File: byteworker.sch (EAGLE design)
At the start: 48 parts, among them IC1 MCP1703, IC2 TJA1043, J1 AVRSPI-62.56-H, Q1 BSS138, Q2 BSS138, Q5 BSS138, Q6 FDN5618P, X1 16 MHz, X2 bus connector

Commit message: unknown changes on IC2
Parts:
- removed C8: 100n, bytewerk-passive:C0603
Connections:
- net +5V: no longer C8.1
- net GND: no longer C8.2
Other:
- moved on the sheet: C7, IC2PWR
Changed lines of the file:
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@@
 <part name="GND10" library="supply1" deviceset="GND" device=""/>
 <part name="C7" library="bytewerk-passive" deviceset="C" device="0603" value="100n"/>
-<part name="C8" library="bytewerk-passive" deviceset="C" device="0603" value="100n"/>
 <part name="GND11" library="supply1" deviceset="GND" device=""/>
-<part name="GND12" library="supply1" deviceset="GND" device=""/>
 <part name="TP1" library="testpad" deviceset="PTR1" device="TP10SQ"/>
 <part name="C3" library="bytewerk-rcl" deviceset="C" device="1206" value="1u/10v"/>
@@
 <instance part="GND15" gate="1" x="106.68" y="50.8"/>
 <instance part="R20" gate="G$1" x="165.1" y="53.34"/>
-<instance part="IC2" gate="PWR" x="10.16" y="71.12" rot="MR0"/>
-<instance part="GND10" gate="1" x="22.86" y="58.42" rot="MR0"/>
-<instance part="C7" gate="G$1" x="27.94" y="66.04" rot="MR270"/>
-<instance part="C8" gate="G$1" x="33.02" y="66.04" rot="MR270"/>
-<instance part="GND11" gate="1" x="27.94" y="58.42" rot="MR0"/>
-<instance part="GND12" gate="1" x="33.02" y="58.42" rot="MR0"/>
+<instance part="IC2" gate="PWR" x="35.56" y="73.66" rot="MR0"/>
+<instance part="GND10" gate="1" x="48.26" y="60.96" rot="MR0"/>
+<instance part="C7" gate="G$1" x="53.34" y="68.58" rot="MR270"/>
+<instance part="GND11" gate="1" x="53.34" y="60.96" rot="MR0"/>
 <instance part="JUMPER1" gate="G$1" x="175.26" y="91.44" rot="R270"/>
 <instance part="D4" gate="G$1" x="218.44" y="81.28" rot="R180"/>
@@
 <segment>
 <pinref part="IC2" gate="PWR" pin="GND"/>
-<wire x1="20.32" y1="68.58" x2="22.86" y2="68.58" width="0.1524" layer="91"/>
-<wire x1="22.86" y1="68.58" x2="22.86" y2="60.96" width="0.1524" layer="91"/>
+<wire x1="45.72" y1="71.12" x2="48.26" y2="71.12" width="0.1524" layer="91"/>
+<wire x1="48.26" y1="71.12" x2="48.26" y2="63.5" width="0.1524" layer="91"/>
 <pinref part="GND10" gate="1" pin="GND"/>
 </segment>
@@
 <pinref part="C7" gate="G$1" pin="2"/>
 <pinref part="GND11" gate="1" pin="GND"/>
-<wire x1="27.94" y1="60.96" x2="27.94" y2="63.5" width="0.1524" layer="91"/>
-</segment>
-<segment>
-<pinref part="C8" gate="G$1" pin="2"/>
-<pinref part="GND12" gate="1" pin="GND"/>
-<wire x1="33.02" y1="60.96" x2="33.02" y2="63.5" width="0.1524" layer="91"/>
+<wire x1="53.34" y1="63.5" x2="53.34" y2="66.04" width="0.1524" layer="91"/>
 </segment>
 <segment>
@@
 </segment>
 <segment>
+<pinref part="IC2" gate="PWR" pin="VIO"/>
+<wire x1="45.72" y1="76.2" x2="53.34" y2="76.2" width="0.1524" layer="91"/>
+<pinref part="C7" gate="G$1" pin="1"/>
+<wire x1="53.34" y1="73.66" x2="53.34" y2="76.2" width="0.1524" layer="91"/>
+<junction x="53.34" y="76.2"/>
 <pinref part="IC2" gate="PWR" pin="VCC"/>
-<wire x1="20.32" y1="76.2" x2="33.02" y2="76.2" width="0.1524" layer="91"/>
-<pinref part="C8" gate="G$1" pin="1"/>
-<wire x1="33.02" y1="76.2" x2="50.8" y2="76.2" width="0.1524" layer="91"/>
-<wire x1="33.02" y1="71.12" x2="33.02" y2="76.2" width="0.1524" layer="91"/>
-<junction x="33.02" y="76.2"/>
-<label x="22.86" y="76.2" size="1.778" layer="95"/>
-</segment>
-<segment>
-<pinref part="IC2" gate="PWR" pin="VIO"/>
-<wire x1="20.32" y1="73.66" x2="27.94" y2="73.66" width="0.1524" layer="91"/>
-<pinref part="C7" gate="G$1" pin="1"/>
-<wire x1="27.94" y1="73.66" x2="50.8" y2="73.66" width="0.1524" layer="91"/>
-<wire x1="27.94" y1="71.12" x2="27.94" y2="73.66" width="0.1524" layer="91"/>
-<junction x="27.94" y="73.66"/>
-<label x="22.86" y="73.66" size="1.778" layer="95"/>
+<wire x1="45.72" y1="78.74" x2="53.34" y2="78.74" width="0.1524" layer="91"/>
+<wire x1="53.34" y1="78.74" x2="58.42" y2="78.74" width="0.1524" layer="91"/>
+<wire x1="58.42" y1="78.74" x2="76.2" y2="78.74" width="0.1524" layer="91"/>
+<label x="48.26" y="78.74" size="1.778" layer="95"/>
+<wire x1="53.34" y1="76.2" x2="53.34" y2="78.74" width="0.1524" layer="91"/>
+<junction x="53.34" y="78.74"/>
 </segment>
 </net>
@@
 <segment>
 <pinref part="IC2" gate="PWR" pin="VBAT"/>
-<wire x1="20.32" y1="78.74" x2="50.8" y2="78.74" width="0.1524" layer="91"/>
-<label x="22.86" y="78.74" size="1.778" layer="95"/>
-</segment>
-<segment>
+<wire x1="45.72" y1="81.28" x2="76.2" y2="81.28" width="0.1524" layer="91"/>
+<label x="48.26" y="81.28" size="1.778" layer="95"/>
+</segment>
+<segment>

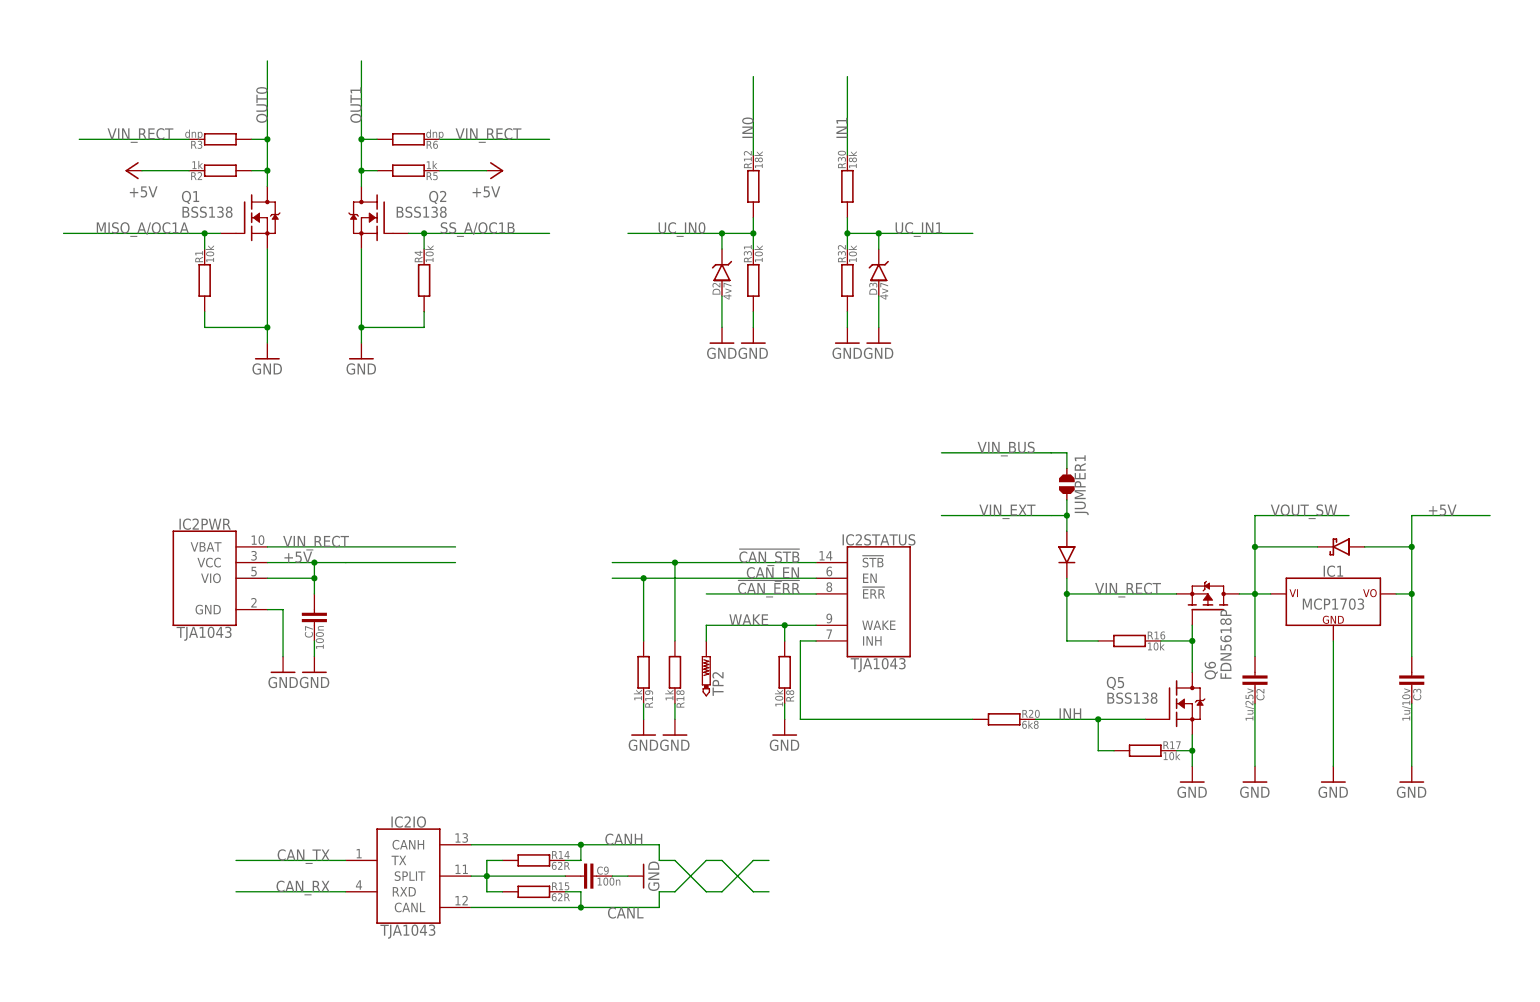
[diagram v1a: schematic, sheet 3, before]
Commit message: - 3rd output fet - moved one ISP pin away from output FET - larger connector with additional ground - larger capacitors - lower part count
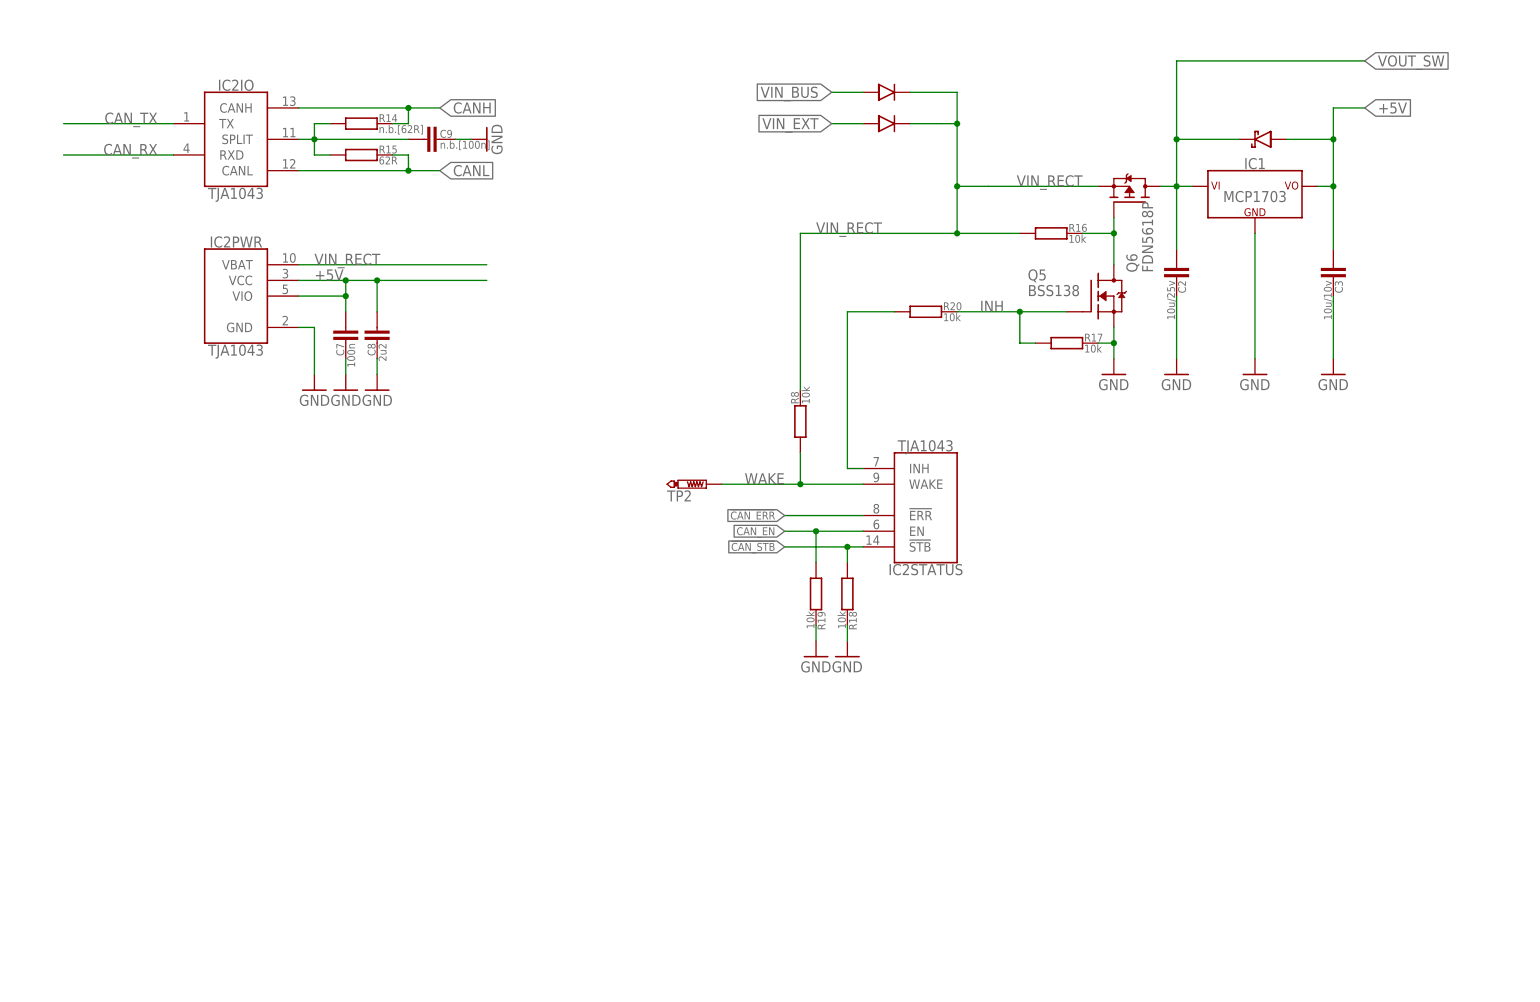
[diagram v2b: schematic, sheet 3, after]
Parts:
- removed JP1: I/O, pinhead:PINHD-2X5/90
- removed JUMPER1: JUMPER-2_10B, bytewerk-jumper:JUMPER-2_10B
- added C8: 2u2, bytewerk-passive:C0805
- added D5: 1N5819HW, bytewerk-passive:1N5819HW
- added JP2: (no value), pinhead:PINHD-2X8/90
- added Q3: BSS138, bytewerk-fet:BSS138
- added R10, R9: 10k, bytewerk-rcl:R0603
- added R11: dnp, bytewerk-rcl:R0603
- added TP3: PTR1TP10SQ, testpad:PTR1TP10SQ
- C2: value 1u/25v -> 10u/25v
- C3: value 1u/10v -> 10u/10v
- C9: value 100n -> n.b.[100n]
- R14: value 62R -> n.b.[62R]
- R18, R19, R2, R5: value 1k -> 10k
- R20: value 6k8 -> 10k
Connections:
- net TXD/MOSI_A/OC0A renamed TXD/MOSI_A/OC0A/SS
- new net N$9: TP3.TP, UC1PORTD.(PSCIN0/CLKO)PD1
- new net OUT2: JP2.9, Q3.D, R10.1, R11.1
- new net PB6: Q1.G, R1.2, UC1PORTB.(ADC7/PSCOUT1B)PB6
- new net PD5/ADC2: JP2.10, UC1PORTD.(ADC2/ACMP2)PD5
- new net PD6/ADC3: JP2.12, UC1PORTD.(ADC3/ACMPN2/INT0)PD6
- new net PD7: Q3.G, R9.2, UC1PORTD.(ACMP0)PD7
- net +5V: now also C8.1, R10.2
- net D2A: now also JP2.14; no longer JP1.10
- net GND: now also C8.2, JP2.16, JP2.2, Q3.S, R9.1; no longer R8.2
- net IN0: now also JP2.4; no longer JP1.6
- net IN1: now also JP2.6; no longer JP1.8
- net MISO_A/OC1A: no longer Q1.G, R1.2
- net OUT0: now also JP2.5; no longer JP1.2
- net OUT1: now also JP2.7; no longer JP1.4
- net PB0/MISO: now also JP2.13; no longer JP1.9
- net PB1/MOSI: now also JP2.15; no longer JP1.7
- net PB7/SCK: now also JP2.11; no longer JP1.5
- net VIN_BUS: now also D5.A; no longer JUMPER1.2
- net VIN_EXT: now also JP2.1; no longer JP1.1, JUMPER1.1
- net VIN_RECT: now also D5.C, R11.2, R8.2
- net VOUT_SW: now also JP2.3; no longer JP1.3
- net WAKE: now also JP2.8
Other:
- note added: "7V to 16V"
- note added: "I/O"
- note added: "MISO/OC1A bereits auf Programmer"
- note removed: "6V to 16V"
- moved on the sheet: C1, C2, C3, C4, C5, C6, C7, C9, IC1, IC2IO, IC2PWR, IC2STATUS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

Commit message: - minor changes to schemanics - placement done(brd)
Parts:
- removed J1: AVRSPI-62.56-H, bytewerk-con:AVRSPI-62.56-H
- removed R7: 1k, bytewerk-passive:R0603
- removed TP1, TP3: PTR1TP10SQ, testpad:PTR1TP10SQ
- added J2: AVRSPI-61.27, bytewerk-con:AVRSPI-61.27
- added JP1, JP3: (no value), pinhead:PINHD-1X10
- added LED2: green, bytewerk-led:LED0603
- added R21, R22: 1k, bytewerk-passive:R0603
- JP2: device pinhead:PINHD-2X8/90 -> pinhead:PINHD-1X8
- X1: device bytewerk-crystal:CRYSTALHC49UP -> bytewerk-crystal:CRYSTAL5X3.2
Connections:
- removed net N$8: LED1.C, R7.1
- removed net N$9: TP3.TP, UC1PORTD.(PSCIN0/CLKO)PD1
- new net N$3: LED2.A, R22.2
- new net PC4: JP3.3, UC1PORTC.(ADC8/AMP1-/ACMPN3)PC4
- new net PD1: JP3.7, UC1PORTD.(PSCIN0/CLKO)PD1
- new net TESTLED1: R21.1, UC1PORTC.(AMP1+/ACMP3/ADC9)PC5
- new net TESTLED2: R22.1, UC1PORTC.(ADC10/ACMP1)PC6
- new net TESTLED3: UC1PORTD.(PSCOUT0A)PD0
- net !RESET!: now also J2.RESET, JP1.10; no longer J1.RESET
- net +5V: now also J2.+5V, JP3.4; no longer J1.+5V
- net AREF: no longer TP1.TP
- net CANH: now also JP3.9
- net CANL: now also JP3.8
- net D2A: now also JP3.6; no longer JP2.14
- net GND: now also J2.GND, JP1.1, JP2.8, LED1.C, LED2.C; no longer J1.GND, JP2.16, JP2.2, R7.2
- net IN0: now also JP2.2; no longer JP2.4
- net IN1: now also JP2.1; no longer JP2.6
- net MISO_A/OC1A: now also J2.MISO, JP1.9; no longer J1.MISO
- net N$7: now also R21.2; no longer UC1PORTD.(PSCOUT0A)PD0
- net OUT0: now also JP2.7; no longer JP2.5
- net OUT1: now also JP2.6; no longer JP2.7
- net OUT2: now also JP2.5; no longer JP2.9
- net PB0/MISO: now also JP1.6; no longer JP2.13
- net PB1/MOSI: now also JP1.5; no longer JP2.15
- net PB7/SCK: now also JP1.4; no longer JP2.11
- net PD5/ADC2: now also JP1.3; no longer JP2.10
- net PD6/ADC3: now also JP1.2; no longer JP2.12
- net RXD/SCK_A: now also J2.SCK, JP1.7; no longer J1.SCK
- net TXD/MOSI_A/OC0A/SS: now also J2.MOSI, JP1.8; no longer J1.MOSI
- net VIN_BUS: now also JP3.5
- net VIN_EXT: now also JP3.1; no longer JP2.1
- net VOUT_SW: now also JP3.2; no longer JP2.3
- net WAKE: now also JP3.10; no longer JP2.8
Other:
- note removed: "MISO/OC1A bereits auf Programmer"
